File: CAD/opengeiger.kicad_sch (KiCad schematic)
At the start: 79 parts, among them J1 Conn_01x02, J10 Conn_01x04, J2 Conn_01x02, J3 Conn_01x06, J4 Conn_01x02, J5 Conn_01x04, J6 Jack-DC, J7 Conn_01x02, J8 USB_C_Receptacle_USB2.0, Q1 STN0214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

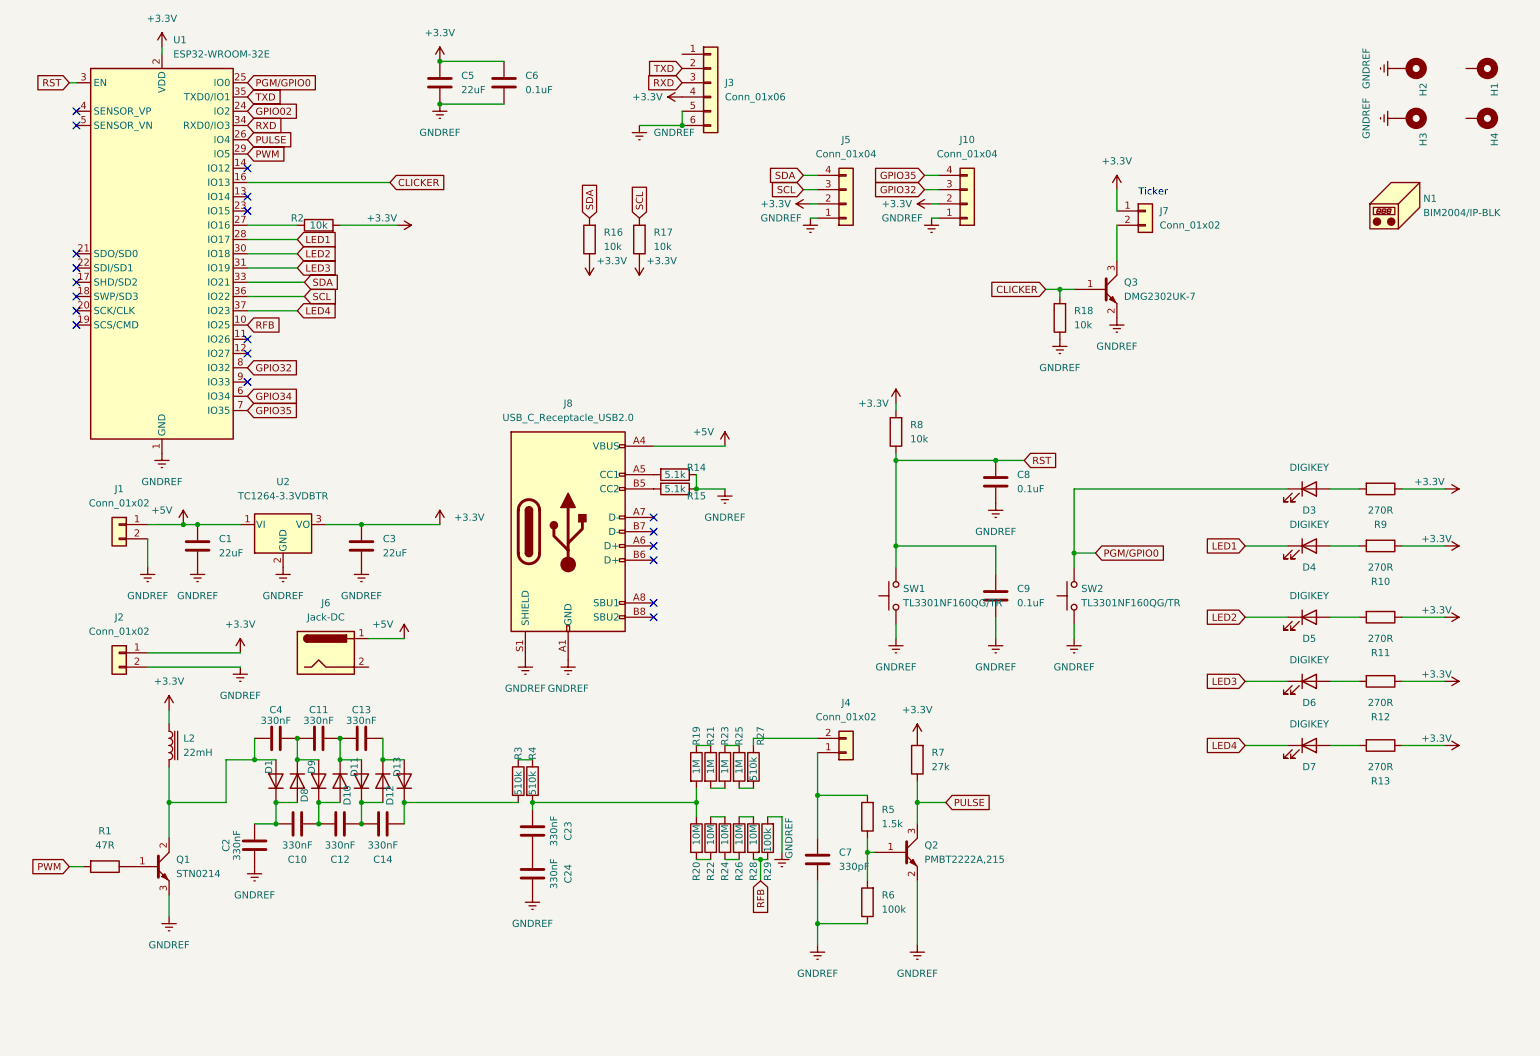
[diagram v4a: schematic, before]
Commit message: Feat: Slimmify more and usb uart
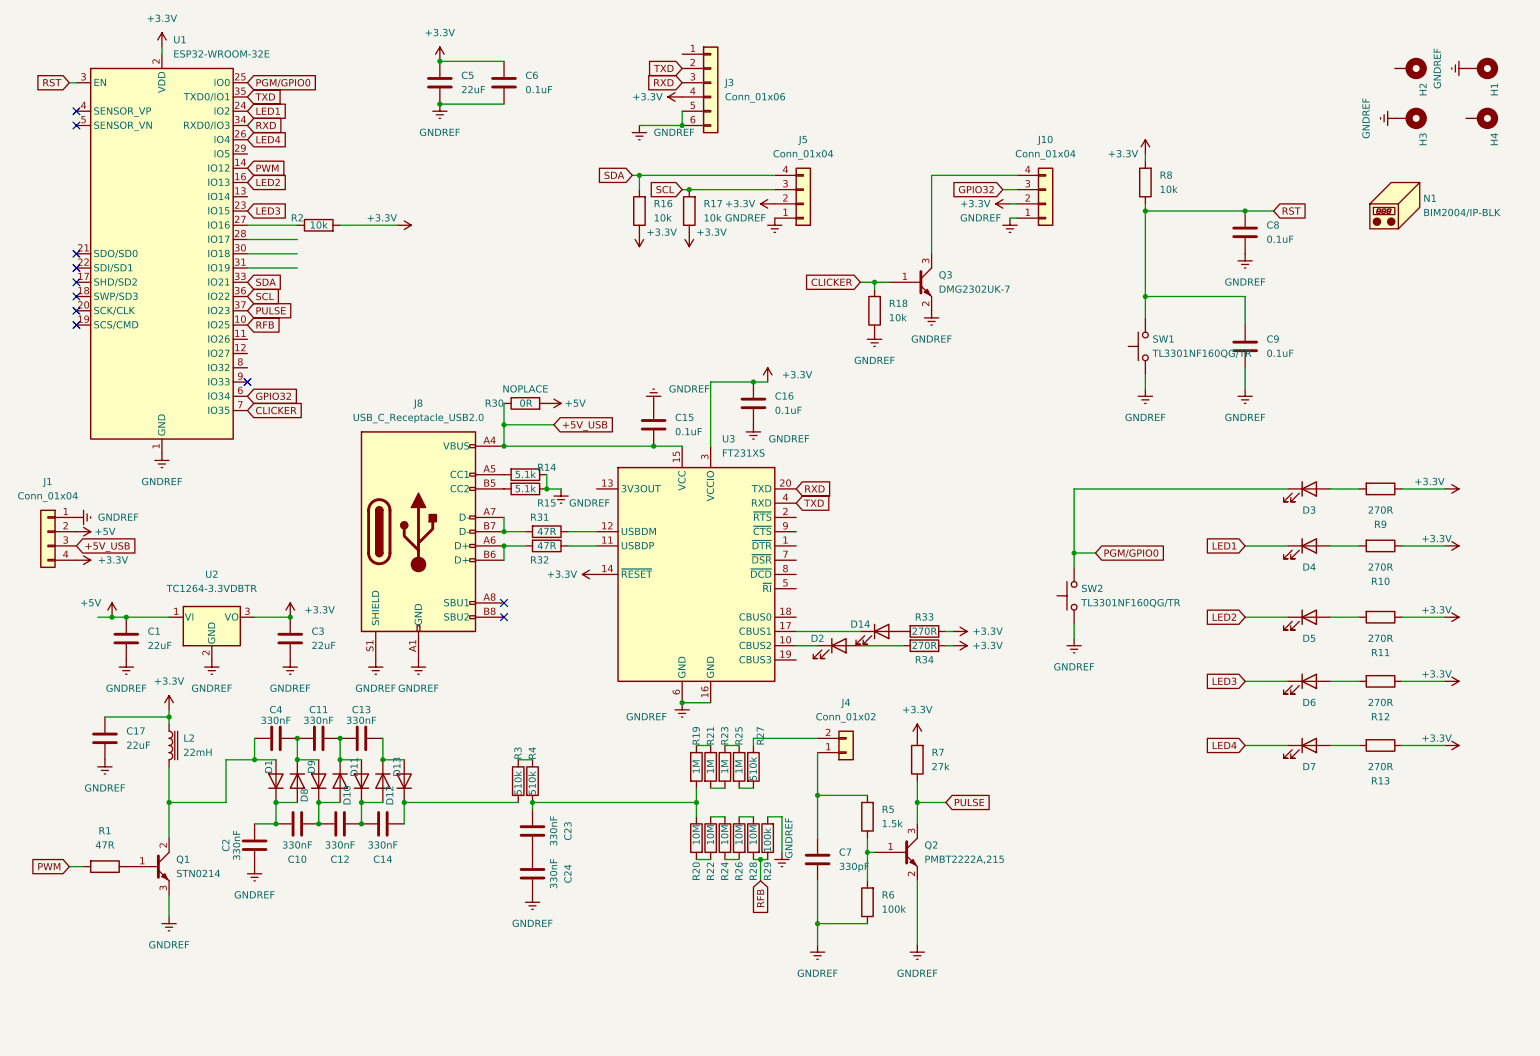
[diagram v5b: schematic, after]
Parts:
- removed J1, J2, J7: Conn_01x02, Fredriklib:TB010-508-02BE, symbol Connector_Generic:Conn_01x02
- removed J6: Jack-DC, symbol Connector:Jack-DC
- added C15, C16: 0.1uF, Capacitor_SMD:C_0603_1608Metric_Pad1.08x0.95mm_HandSolder, symbol Device:C
- added C17: 22uF, Capacitor_SMD:C_0805_2012Metric_Pad1.18x1.45mm_HandSolder, symbol Device:C
- added D14, D2: 0603RBD0700S01, LED_SMD:LED_0603_1608Metric, symbol Device:LED
- added J1: Conn_01x04, Connector_PinHeader_2.54mm:PinHeader_1x04_P2.54mm_Vertical, symbol Connector_Generic:Conn_01x04
- added R30: 0R, Resistor_SMD:R_1206_3216Metric_Pad1.30x1.75mm_HandSolder, symbol Device:R
- added R31, R32: 47R, Resistor_SMD:R_0603_1608Metric_Pad0.98x0.95mm_HandSolder, symbol Device:R
- added R33, R34: 270R, Resistor_SMD:R_0603_1608Metric_Pad0.98x0.95mm_HandSolder, symbol Device:R
- added U3: FT231XS, Package_SO:SSOP-20_3.9x8.7mm_P0.635mm, symbol Interface_USB:FT231XS
- D1, D10, D11, D12, D13, D8, D9: footprint Diode_SMD:D_SMA_Handsoldering -> Diode_SMD:D_SMA
- H1, H2, H3: footprint MountingHole:MountingHole_2.5mm_Pad -> MountingHole:MountingHole_2.5mm_Pad_Via
- H4: footprint MountingHole:MountingHole_2.5mm_Pad -> MountingHole:MountingHole_2.7mm
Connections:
- net GPIO02 is gone; now on net LED1: U1.24 (IO2)
- net GPIO34 is gone; now on net GPIO32: U1.6 (IO34)
- net +3.3V: now also C16.1, C17.1, J1.4 (Pin_4), R33.1, R34.1, U3.14 (~{RESET}), U3.3 (VCCIO)
- net +5V: now also J1.2 (Pin_2), R30.2; no longer J8.A4 (VBUS), J8.A9 (VBUS), J8.B4 (VBUS), J8.B9 (VBUS)
- net CLICKER: now also U1.7 (IO35); no longer U1.16 (IO13)
- net GNDREF: now also H1.1, C15.1, C16.2, C17.2, J1.1 (Pin_1), U3.16 (GND), U3.6 (GND); no longer H2.1
- net GPIO32: no longer U1.8 (IO32)
- net LED1: no longer U1.28 (IO17)
- net LED2: now also U1.16 (IO13); no longer U1.30 (IO18)
- net LED3: now also U1.23 (IO15); no longer U1.31 (IO19)
- net LED4: now also U1.26 (IO4); no longer U1.37 (IO23)
- net PULSE: now also U1.37 (IO23); no longer U1.26 (IO4)
- net PWM: now also U1.14 (IO12); no longer U1.29 (IO5)
- net RXD: now also U3.20 (TXD)
- net TXD: now also U3.4 (RXD)
- net at Q3.3 (C): now also J10.4 (Pin_4)
- net at J8.A6 (D+): now also J8.B6 (D+), R32.2
- net at J8.A7 (D-): now also J8.B7 (D-), R31.2
- removed net GPIO35: J10.4 (Pin_4), U1.7 (IO35)
- new net: D2.2 (A), R34.2
- new net: D2.1 (K), U3.10 (CBUS2)
- new net: R32.1, U3.11 (USBDP)
- new net: D14.2 (A), R33.2
- new net: R31.1, U3.12 (USBDM)
- new net: D14.1 (K), U3.17 (CBUS1)
- new net +5V_USB: C15.2, J1.3 (Pin_3), J8.A4 (VBUS), J8.A9 (VBUS), J8.B4 (VBUS), J8.B9 (VBUS), R30.1, U3.15 (VCC)
- no-connect marks 20 -> 11
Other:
- note removed: "Ticker"
- moved on the sheet: C1, C3, C8, C9, J10, J5, J8, Q3, R14, R15, R16, R17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

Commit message: Feat:WIP Rounding tracks
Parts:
- removed J4: Conn_01x02, Fredriklib:TB010-508-02BE, symbol Connector_Generic:Conn_01x02
- added FID1, FID2, FID3: Fiducial, Fiducial:Fiducial_1mm_Mask2mm, symbol Mechanical:Fiducial
- added G1: GM_tube_HOLDERS, eikgeiger:SBM-20, symbol Sensor:Nuclear-Radiation_Detector
- added Q4: UMH3N, Package_TO_SOT_SMD:SOT-363_SC-70-6, symbol Transistor_BJT:UMH3N
- H2: footprint MountingHole:MountingHole_2.5mm_Pad_Via -> MountingHole:MountingHole_2.5mm
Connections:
- net PGM/GPIO0: now also Q4.3 (C2)
- net RST: now also Q4.6 (C1)
- net HV_A: now reaches C14.2, D13.1 (K), R3.2
- net HV_B: now reaches C23.2, R19.2, R20.1, R4.2
- net SWITCH: now reaches C4.1, D1.2 (A), L2.2, Q1.2 (C), Q1.4 (C)
- net CBUS2: now reaches D2.1 (K), U3.10 (CBUS2)
- net DP: now reaches R32.1, U3.11 (USBDP)
- net DP*: now reaches J8.A6 (D+), J8.B6 (D+), R32.2
- net DTR#: now reaches U3.1 (~{DTR})
- net DTR#: now also Q4.2 (B1), Q4.4 (E2)
- net DM: now reaches R31.1, U3.12 (USBDM)
- net CBUS1: now reaches D14.1 (K), U3.17 (CBUS1)
- net RTS#: now reaches U3.2 (~{RTS})
- net RTS#: now also Q4.1 (E1), Q4.5 (B2)
- net HV_C: now reaches R27.1
- net HV_C: now also G1.1
- net at C7.1, R5.2: now also G1.2
- net DM*: now reaches J8.A7 (D-), J8.B7 (D-), R31.2
- net CC2: now reaches J8.B5 (CC2), R15.2
- net CC1: now reaches J8.A5 (CC1), R14.2
- no-connect marks 11 -> 17
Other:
- moved on the sheet: C7, D14, D2, R14, R15, R19, R20, R21, R22, R23, R24, R25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

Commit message: Feat: Production files for JLC prod, readme update
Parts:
- removed N1: BIM2004/IP-BLK, symbol Mechanical:Housing
- SW1, SW2: footprint Button_Switch_SMD:SW_SPST_PTS645 -> eikgeiger:SW_TL3301NF160QG_TR
- U1: footprint RF_Module:ESP32-WROOM-32 -> eikgeiger:ESP32-WROOM-32
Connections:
- no-connect marks 17 -> 30
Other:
- moved on the sheet: C10, C11, C12, C13, C14, C17, C2, C23, C24, C4, C7, D1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

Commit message: Feat: New prod, working code
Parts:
- H4: footprint MountingHole:MountingHole_2.7mm -> MountingHole:MountingHole_2.5mm
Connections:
- net +3.3V: no longer U3.14 (~{RESET})
- net CLICKER: now also U1.8 (IO32); no longer U1.7 (IO35)
- net GPIO32: now also U1.9 (IO33); no longer U1.6 (IO34)
- net 3v3fdti: now reaches U3.13 (3V3OUT)
- net 3v3fdti: now also U3.14 (~{RESET})
- no-connect marks 30 -> 29
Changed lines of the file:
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@@
   (junction (at 110.49 97.79) (diameter 0) (color 0 0 0 0)
   )
-  (no_connect (at 53.34 76.2))
+  (no_connect (at 53.34 81.28))
   (no_connect (at 53.34 73.66))
   (no_connect (at 53.34 71.12))
@@
   (no_connect (at 151.13 128.27))
   (no_connect (at 130.81 20.32))
-  (no_connect (at 115.57 97.79))
   (no_connect (at 22.86 68.58))
   (no_connect (at 22.86 55.88))
@@
   (no_connect (at 99.06 120.65))
   (no_connect (at 130.81 22.86))
-  (no_connect (at 53.34 78.74))
+  (no_connect (at 53.34 83.82))
   (no_connect (at 270.51 31.75))
   (no_connect (at 257.81 22.86))
@@
     (stroke (width 0) (type default) (color 0 0 0 0))
   )
+  (wire (pts (xy 115.57 92.0242) (xy 112.2756 92.0242))
+    (stroke (width 0) (type default) (color 0 0 0 0))
+  )
   (wire (pts (xy 125.73 90.17) (xy 130.81 90.17))
     (stroke (width 0) (type default) (color 0 0 0 0))
@@
     (stroke (width 0) (type default) (color 0 0 0 0))
   )
+  (wire (pts (xy 115.57 97.79) (xy 115.57 92.0242))
+    (stroke (width 0) (type default) (color 0 0 0 0))
+  )
   (wire (pts (xy 69.85 156.21) (xy 73.66 156.21))
     (stroke (width 0) (type default) (color 0 0 0 0))
@@
     )
   )
-  (global_label "CLICKER" (shape input) (at 53.34 83.82 0) (fields_autoplaced)
-    (effects (font (size 1.27 1.27)) (justify left))
-    (property "Intersheet References" "${INTERSHEET_REFS}" (id 0) (at 63.615 83.8994 0)
-      (effects (font (size 1.27 1.27)) (justify left) hide)
-    )
-  )
   (global_label "RTS#" (shape input) (at 151.13 102.87 0) (fields_autoplaced)
     (effects (font (size 1.27 1.27)) (justify left))
@@
     )
   )
+  (global_label "CLICKER" (shape input) (at 53.34 76.2 0) (fields_autoplaced)
+    (effects (font (size 1.27 1.27)) (justify left))
+    (property "Intersheet References" "${INTERSHEET_REFS}" (id 0) (at 63.615 76.2794 0)
+      (effects (font (size 1.27 1.27)) (justify left) hide)
+    )
+  )
   (global_label "PGM{slash}GPIO0" (shape input) (at 204.47 109.22 0) (fields_autoplaced)
     (effects (font (size 1.27 1.27)) (justify left))
@@
     )
   )
+  (global_label "3v3fdti" (shape input) (at 112.2756 92.0242 180) (fields_autoplaced)
+    (effects (font (size 1.27 1.27)) (justify right))
+    (property "Intersheet References" "${INTERSHEET_REFS}" (id 0) (at 103.2706 91.9448 0)
+      (effects (font (size 1.27 1.27)) (justify right) hide)
+    )
+  )
   (global_label "RST" (shape input) (at 168.91 97.79 90) (fields_autoplaced)
     (effects (font (size 1.27 1.27)) (justify left))
@@
     )
   )
+  (global_label "3v3fdti" (shape input) (at 115.57 113.03 180) (fields_autoplaced)
+    (effects (font (size 1.27 1.27)) (justify right))
+    (property "Intersheet References" "${INTERSHEET_REFS}" (id 0) (at 106.565 112.9506 0)
+      (effects (font (size 1.27 1.27)) (justify right) hide)
+    )
+  )
   (global_label "PWM" (shape input) (at 21.59 175.26 180) (fields_autoplaced)
     (effects (font (size 1.27 1.27)) (justify right))
@@
     )
   )
-  (global_label "GPIO32" (shape input) (at 53.34 81.28 0) (fields_autoplaced)
+  (global_label "GPIO32" (shape input) (at 53.34 78.74 0) (fields_autoplaced)
     (effects (font (size 1.27 1.27)) (justify left))
-    (property "Intersheet References" "${INTERSHEET_REFS}" (id 0) (at 62.6474 81.3594 0)
+    (property "Intersheet References" "${INTERSHEET_REFS}" (id 0) (at 62.6474 78.8194 0)
       (effects (font (size 1.27 1.27)) (justify left) hide)
     )
@@
       (effects (font (size 1.27 1.27)) (justify left) hide)
     )
-    (property "Footprint" "MountingHole:MountingHole_2.7mm" (id 2) (at 273.05 31.75 0)
+    (property "Footprint" "MountingHole:MountingHole_2.5mm" (id 2) (at 273.05 31.75 0)
       (effects (font (size 1.27 1.27)) hide)
     )
@@
     (pin "1")
   )
-  (symbol (lib_id "power:+3.3V") (at 115.57 113.03 90) (unit 1)
-    (in_bom yes) (on_board yes)
-    (property "Reference" "#PWR0114" (id 0) (at 119.38 113.03 0)
-      (effects (font (size 1.27 1.27)) hide)
-    )
-    (property "Value" "+3.3V" (id 1) (at 106.68 113.03 90)
-      (effects (font (size 1.27 1.27)) (justify right))
-    )
-    (property "Footprint" "" (id 2) (at 115.57 113.03 0)
-      (effects (font (size 1.27 1.27)) hide)
-    )
-    (property "Datasheet" "" (id 3) (at 115.57 113.03 0)
-      (effects (font (size 1.27 1.27)) hide)
-    )
-    (pin "1")
-  )
   (symbol (lib_id "Device:R") (at 255.27 143.51 270) (unit 1)
     (in_bom yes) (on_board yes) (fields_autoplaced)
@@
   (symbol (lib_id "Device:R") (at 106.68 95.25 270) (unit 1)
     (in_bom yes) (on_board yes)
-    (property "Reference" "R14" (id 0) (at 110.49 93.98 90))
+    (property "Reference" "R14" (id 0) (at 111.4568 94.4261 90))
     (property "Value" "5.1k" (id 1) (at 106.68 95.25 90))
     (property "Footprint" "Resistor_SMD:R_0603_1608Metric_Pad0.98x0.95mm_HandSolder" (id 2) (at 106.68 93.472 90)
@@
       (reference "#PWR0113") (unit 1) (value "GNDREF") (footprint "")
     )
-    (path "/9c7783a1-b5cd-48c6-b783-09d3dd2be4d2"
-      (reference "#PWR0114") (unit 1) (value "+3.3V") (footprint "")
-    )
     (path "/c21c3f9c-b954-4ac9-8eaa-fbc5063590fa"
       (reference "#PWR0115") (unit 1) (value "+3.3V") (footprint "")
@@
     )
     (path "/6c3028cf-5bcc-4a06-8a3b-d0ff1fd6e557"
-      (reference "H4") (unit 1) (value "MountingHole_Pad") (footprint "MountingHole:MountingHole_2.7mm")
+      (reference "H4") (unit 1) (value "MountingHole_Pad") (footprint "MountingHole:MountingHole_2.5mm")
     )
     (path "/a6d5da21-3138-4dd2-a8d1-9af5fa4fde9e"
